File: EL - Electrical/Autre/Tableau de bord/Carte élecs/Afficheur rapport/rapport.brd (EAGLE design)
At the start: 64 x 40 mm, 15 parts, among them IC1 MCP23008P, X1 22-23-2041

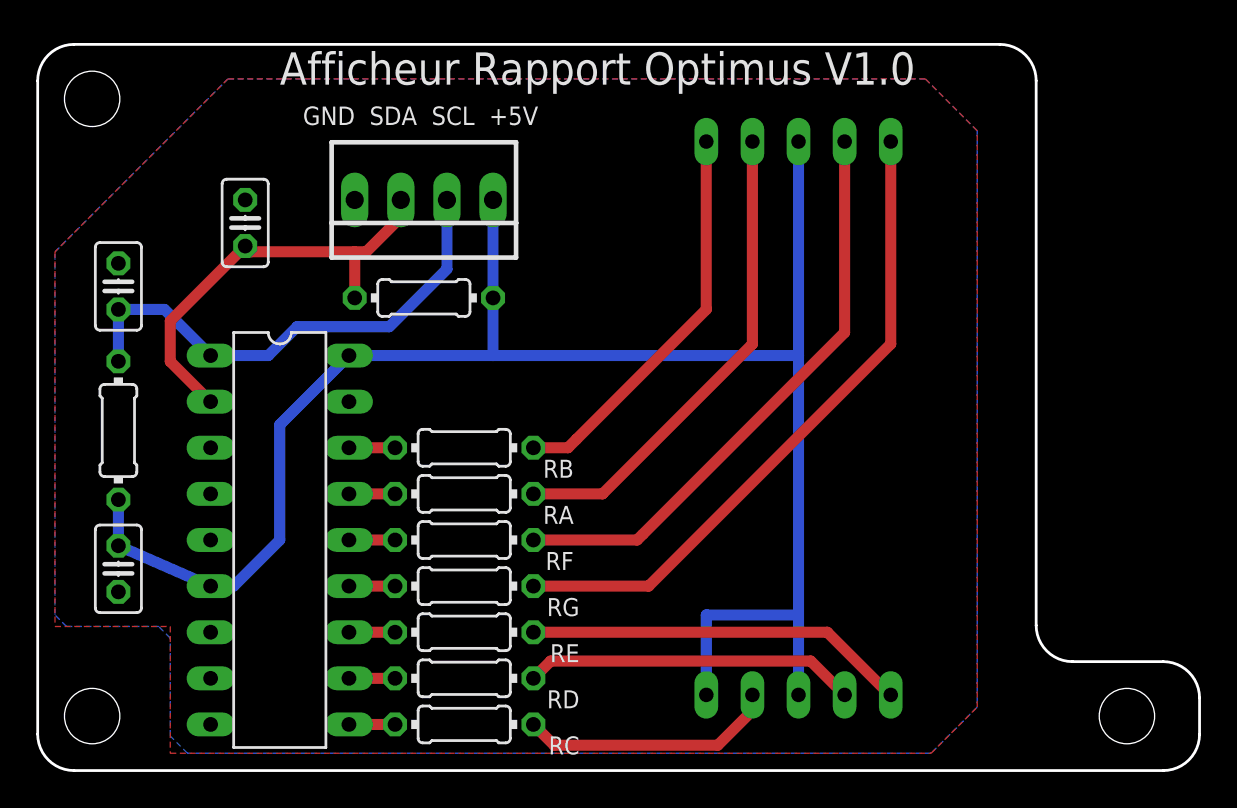
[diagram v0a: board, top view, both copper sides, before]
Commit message: modif afficheur rapport
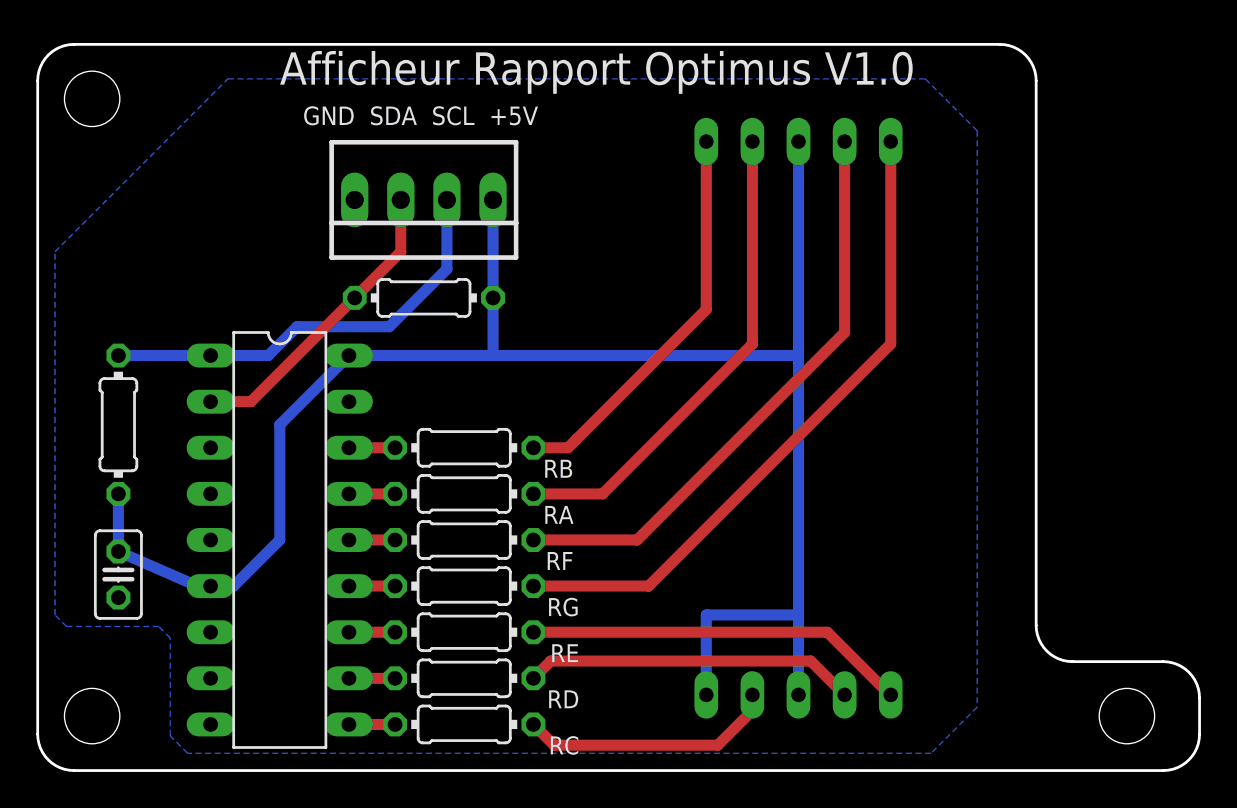
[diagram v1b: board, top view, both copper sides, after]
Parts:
- removed C2: 135pF, rcl:C025-025X050
- removed C3: 135 pF, rcl:C025-025X050
- moved C1 0.32 mm to (4.45, 10.8)
- moved R2 0.32 mm to (4.45, 19.1)
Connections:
- net GND: no longer C2.2, C3.2
- net SCL: no longer C3.1
- net SDA: no longer C2.1
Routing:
- net SDA: track 24.2 -> 16.8 mm
- net SCL: track 27.8 -> 23.9 mm
- net +5V: track 98.0 -> 98.6 mm
- removed copper zone on layer 1, net GND
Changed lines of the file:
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@@
 </autorouter>
 <elements>
-<element name="C1" library="rcl" library_urn="urn:adsk.eagle:library:334" package="C025-025X050" package3d_urn="urn:adsk.eagle:package:23629/2" value="500pF" x="4.445" y="11.1125" smashed="yes" rot="R270">
-<attribute name="SPICEPREFIX" value="C" x="4.445" y="11.1125" size="1.778" layer="27" rot="R270" display="off"/>
-<attribute name="VALUE" x="2.4765" y="8.509" size="1.27" layer="27" ratio="10" rot="R90"/>
-</element>
-<element name="C2" library="rcl" library_urn="urn:adsk.eagle:library:334" package="C025-025X050" package3d_urn="urn:adsk.eagle:package:23629/2" value="135pF" x="11.43" y="30.1625" smashed="yes" rot="R90">
-<attribute name="SPICEPREFIX" value="C" x="11.43" y="30.1625" size="1.778" layer="27" rot="R90" display="off"/>
-<attribute name="VALUE" x="9.4615" y="27.8765" size="1.27" layer="27" ratio="10" rot="R90"/>
-</element>
-<element name="C3" library="rcl" library_urn="urn:adsk.eagle:library:334" package="C025-025X050" package3d_urn="urn:adsk.eagle:package:23629/2" value="135 pF" x="4.445" y="26.67" smashed="yes" rot="R90">
-<attribute name="SPICEPREFIX" value="C" x="4.445" y="26.67" size="1.778" layer="27" rot="R90" display="off"/>
-<attribute name="VALUE" x="2.4765" y="24.0665" size="1.27" layer="27" ratio="10" rot="R90"/>
+<element name="C1" library="rcl" library_urn="urn:adsk.eagle:library:334" package="C025-025X050" package3d_urn="urn:adsk.eagle:package:23629/2" value="500pF" x="4.445" y="10.795" smashed="yes" rot="R270">
+<attribute name="SPICEPREFIX" value="C" x="4.445" y="10.795" size="1.778" layer="27" rot="R270" display="off"/>
+<attribute name="VALUE" x="2.4765" y="8.1915" size="1.27" layer="27" ratio="10" rot="R90"/>
 </element>
 <element name="IC1" library="microchip-dspic" package="DIL18" value="MCP23008P" x="13.335" y="12.7" smashed="yes" rot="R270">
@@
 <attribute name="VALUE" x="20.5994" y="25.5524" size="0.9906" layer="27" ratio="10"/>
 </element>
-<element name="R2" library="rcl" library_urn="urn:adsk.eagle:library:334" package="0204/7" package3d_urn="urn:adsk.eagle:package:23498/1" value="1k" x="4.445" y="18.7325" smashed="yes" rot="R90">
-<attribute name="SPICEPREFIX" value="R" x="4.445" y="18.7325" size="1.778" layer="27" rot="R90" display="off"/>
-<attribute name="VALUE" x="4.9276" y="18.0594" size="0.9906" layer="27" ratio="10" rot="R90"/>
+<element name="R2" library="rcl" library_urn="urn:adsk.eagle:library:334" package="0204/7" package3d_urn="urn:adsk.eagle:package:23498/1" value="1k" x="4.445" y="19.05" smashed="yes" rot="R90">
+<attribute name="SPICEPREFIX" value="R" x="4.445" y="19.05" size="1.778" layer="27" rot="R90" display="off"/>
+<attribute name="VALUE" x="4.9276" y="18.3769" size="0.9906" layer="27" ratio="10" rot="R90"/>
 </element>
 <element name="X1" library="con-molex" library_urn="urn:adsk.eagle:library:165" package="22-23-2041" value="22-23-2041" x="21.2725" y="31.4325" smashed="yes" rot="R180">
@@
 <contactref element="IC1" pad="3"/>
 <contactref element="IC1" pad="4"/>
-<contactref element="C2" pad="2"/>
-<contactref element="C3" pad="2"/>
 <contactref element="X1" pad="4"/>
-<polygon width="0.254" layer="1">
-<vertex x="0.9525" y="7.9375"/>
-<vertex x="7.3025" y="7.9375"/>
-<vertex x="7.3025" y="0.9525"/>
-<vertex x="49.2125" y="0.9525"/>
-<vertex x="51.7525" y="3.4925"/>
-<vertex x="51.7525" y="35.2425"/>
-<vertex x="48.895" y="38.1"/>
-<vertex x="10.4775" y="38.1"/>
-<vertex x="0.9525" y="28.575"/>
-</polygon>
 <polygon width="0.1524" layer="16">
 <vertex x="1.5875" y="7.9375"/>
@@
 <contactref element="X1" pad="1"/>
 <wire x1="25.0825" y1="31.4325" x2="25.0825" y2="26.035" width="0.6096" layer="16"/>
-<wire x1="4.445" y1="12.3825" x2="9.525" y2="10.16" width="0.6096" layer="16"/>
+<wire x1="8.799284375" y1="10.16" x2="9.525" y2="10.16" width="0.6096" layer="16"/>
+<wire x1="8.799284375" y1="10.16" x2="4.445" y2="12.065" width="0.6096" layer="16"/>
 <wire x1="9.525" y1="10.16" x2="10.795" y2="10.16" width="0.6096" layer="16"/>
 <wire x1="10.795" y1="10.16" x2="13.335" y2="12.7" width="0.6096" layer="16"/>
@@
 <contactref element="LED1" pad="8"/>
 <contactref element="LED1" pad="3"/>
-<wire x1="4.445" y1="14.9225" x2="4.445" y2="12.3825" width="0.6096" layer="16"/>
+<wire x1="4.445" y1="15.24" x2="4.445" y2="12.065" width="0.6096" layer="16"/>
 <wire x1="41.91" y1="34.6475" x2="41.91" y2="22.86" width="0.6096" layer="16"/>
 <wire x1="41.91" y1="22.86" x2="41.91" y2="8.5725" width="0.6096" layer="16"/>
@@
 <signal name="SCL">
 <contactref element="R2" pad="2"/>
-<contactref element="C3" pad="1"/>
 <contactref element="IC1" pad="1"/>
 <contactref element="X1" pad="2"/>
@@
 <wire x1="14.2875" y1="24.4475" x2="12.7" y2="22.86" width="0.6096" layer="16"/>
 <wire x1="12.7" y1="22.86" x2="9.525" y2="22.86" width="0.6096" layer="16"/>
-<wire x1="4.445" y1="22.5425" x2="4.445" y2="25.4" width="0.6096" layer="16"/>
 <wire x1="22.5425" y1="31.4325" x2="22.5425" y2="27.6225" width="0.6096" layer="16"/>
-<wire x1="9.525" y1="22.86" x2="6.985" y2="25.4" width="0.6096" layer="16"/>
-<wire x1="6.985" y1="25.4" x2="4.445" y2="25.4" width="0.6096" layer="16"/>
+<wire x1="9.525" y1="22.86" x2="4.445" y2="22.86" width="0.6096" layer="16"/>
 </signal>
 <signal name="N$10">
@@
 <signal name="SDA">
 <contactref element="IC1" pad="2"/>
-<contactref element="C2" pad="1"/>
 <contactref element="R1" pad="1"/>
 <contactref element="X1" pad="3"/>
-<wire x1="7.3025" y1="22.5298625" x2="9.5123625" y2="20.32" width="0.6096" layer="1"/>
-<wire x1="9.5123625" y1="20.32" x2="9.525" y2="20.32" width="0.1524" layer="1"/>
-<wire x1="17.4625" y1="28.575" x2="18.0975" y2="28.575" width="0.6096" layer="1"/>
-<wire x1="17.4625" y1="28.575" x2="11.7475" y2="28.575" width="0.6096" layer="1"/>
-<wire x1="11.7475" y1="28.575" x2="11.43" y2="28.8925" width="0.6096" layer="1"/>
-<wire x1="11.43" y1="28.8925" x2="7.3025" y2="24.765" width="0.6096" layer="1"/>
-<wire x1="7.3025" y1="24.765" x2="7.3025" y2="22.5298625" width="0.6096" layer="1"/>
-<wire x1="17.4625" y1="26.035" x2="17.4625" y2="28.575" width="0.6096" layer="1"/>
-<wire x1="18.0975" y1="28.575" x2="20.0025" y2="30.48" width="0.6096" layer="1"/>
-<wire x1="20.0025" y1="30.48" x2="20.0025" y2="31.4325" width="0.6096" layer="1"/>
+<wire x1="9.525" y1="20.32" x2="11.7475" y2="20.32" width="0.6096" layer="1"/>
+<wire x1="11.7475" y1="20.32" x2="17.4625" y2="26.035" width="0.6096" layer="1"/>
+<wire x1="17.4625" y1="26.035" x2="20.0025" y2="28.575" width="0.6096" layer="1"/>
+<wire x1="20.0025" y1="28.575" x2="20.0025" y2="31.4325" width="0.6096" layer="1"/>
 </signal>
 <signal name="GP6">
